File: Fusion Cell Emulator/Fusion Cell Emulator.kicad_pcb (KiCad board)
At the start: 2 copper layers, 116.8 x 190.5 mm, 120 parts, among them J1 BINDING_POST_RED, J2 BINDING_POST_BLACK, J3 JST-XH, J4 0.1" FEMALE HEADER, J6 BINDING_POST_RED, J7 BINDING_POST_BLACK, U1 LM317, U10 LM317, U11 LM317, U12 LM317, U13 LM317, U2 LM317, U3 LM317, U4 LM317, U5 LM317, U6 LM317, U7 LM317, U8 LM317, U9 LM317

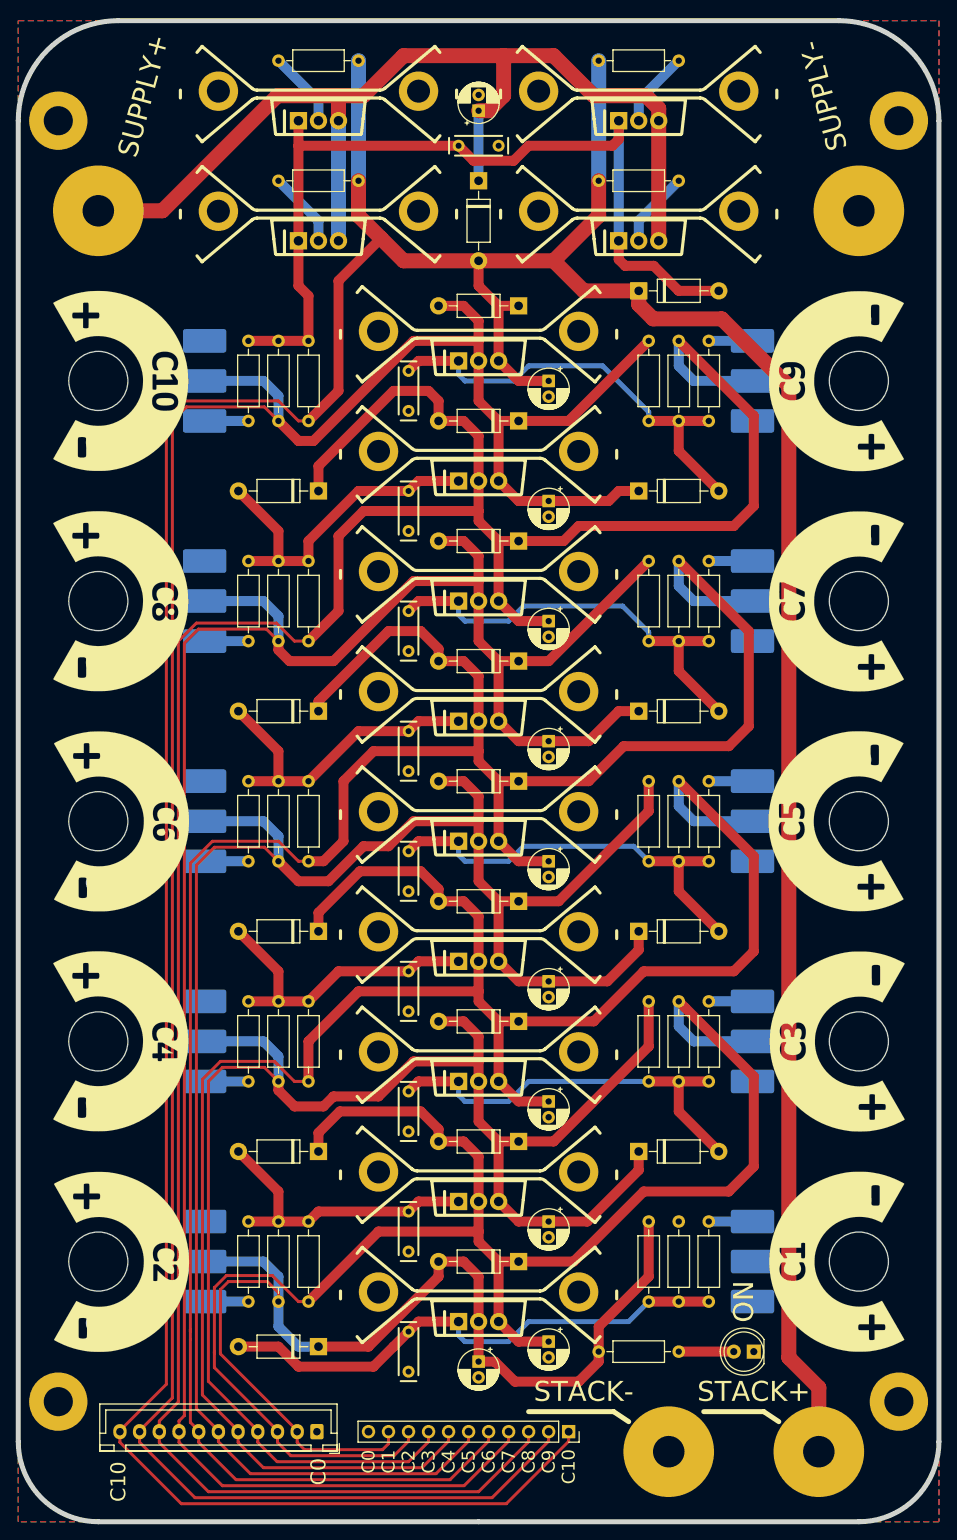
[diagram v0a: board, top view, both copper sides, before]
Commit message: Fixing silk screen and updating gerbers
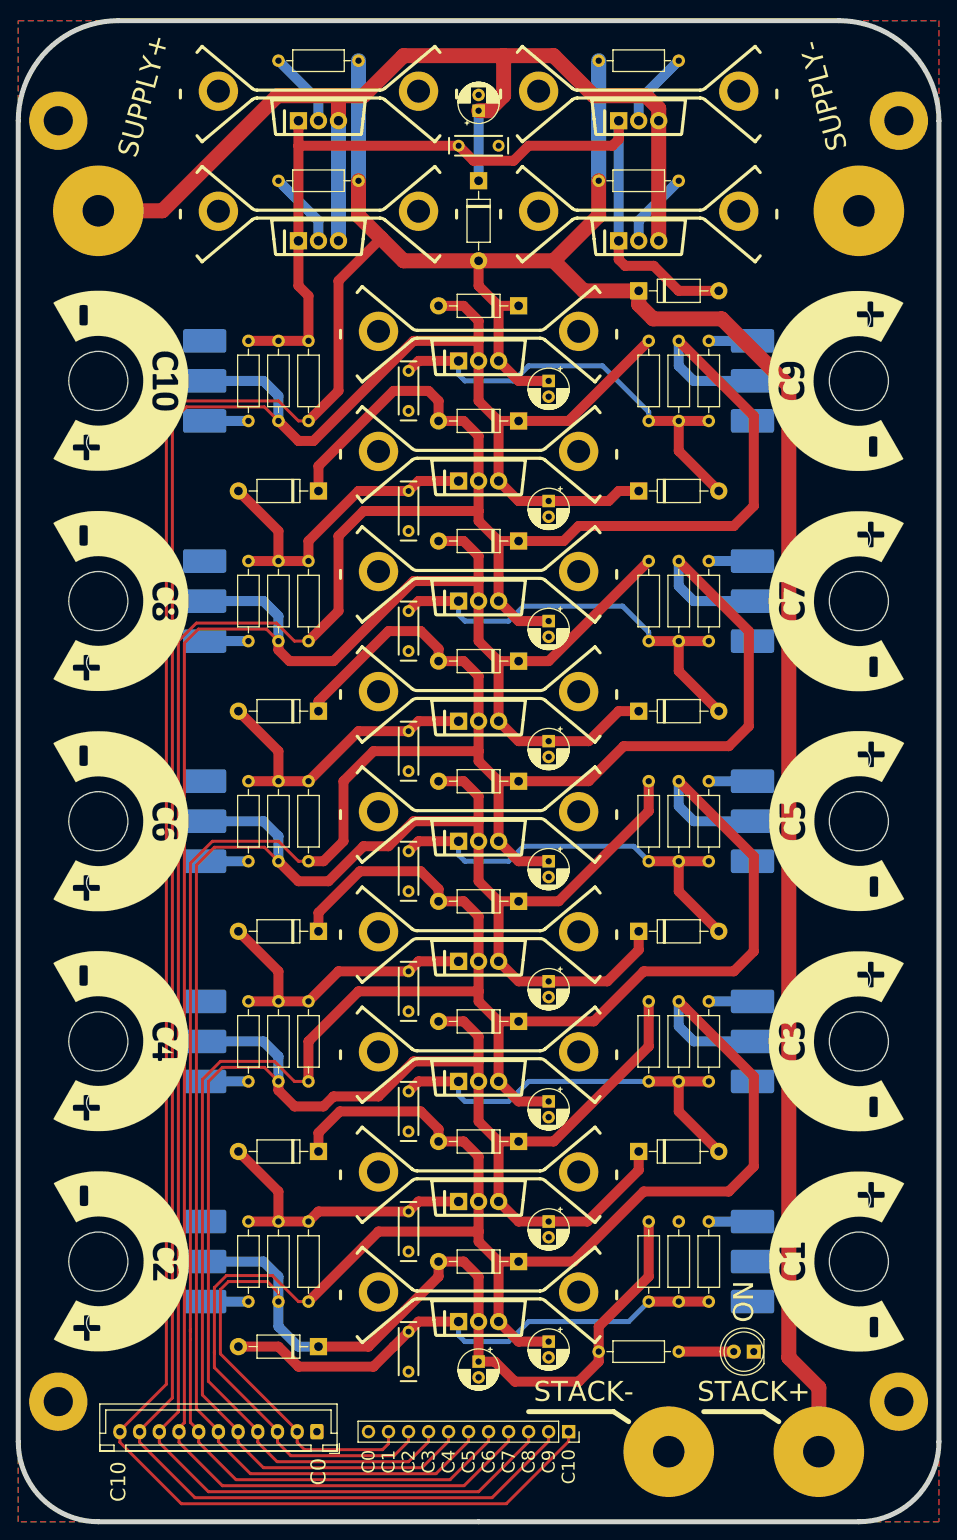
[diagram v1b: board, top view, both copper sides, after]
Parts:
- removed the G*** at (201.0, 103.2)
- removed the G*** at (103.8, -6.70)
- removed the G*** at (201.1, 75.3)
- removed the G*** at (200.9, 47.4)
- removed the G*** at (200.9, 19.4)
- removed the G*** at (200.9, -8.50)
- removed the G*** at (104.0, 105.1)
- removed the G*** at (103.8, 77.1)
- removed the G*** at (104.0, 49.2)
- removed the G*** at (103.8, 21.2)
- added G***: LOGO, Custom-Graphics:Cell_Graphic_Invert_C1, F.Cu at (200.9, 105.0)
- added G***: LOGO, Custom-Graphics:Cell_Graphic_Invert_C10, F.Cu at (104.0, -8.45)
- added G***: LOGO, Custom-Graphics:Cell_Graphic_Invert_C3, F.Cu at (200.8, 77.0)
- added G***: Cell_Graphic_Invert_C5, Custom-Graphics:Cell_Graphic_Invert_C5, F.Cu at (200.9, 49.0)
- added G***: LOGO, Custom-Graphics:Cell_Graphic_Invert_C7, F.Cu at (200.8, 21.1)
- added G***: LOGO, Custom-Graphics:Cell_Graphic_Invert_C9, F.Cu at (200.8, -6.80)
- added G***: LOGO, Custom-Graphics:Cell_Graphic_Invert_C2, F.Cu at (104.0, 103.3)
- added G***: LOGO, Custom-Graphics:Cell_Graphic_Invert_C4, F.Cu at (104.0, 75.3)
- added G***: LOGO, Custom-Graphics:Cell_Graphic_Invert_C6, F.Cu at (104.0, 47.5)
- added G***: LOGO, Custom-Graphics:Cell_Graphic_Invert_C8, F.Cu at (104.0, 19.5)

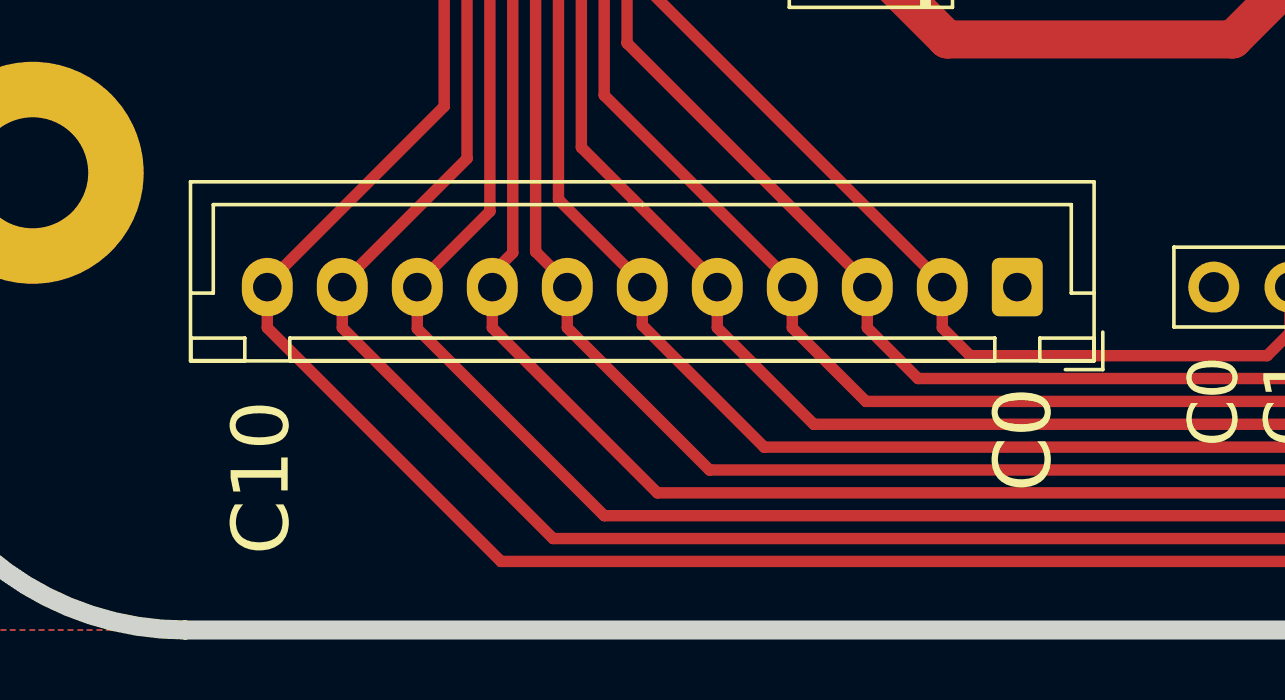
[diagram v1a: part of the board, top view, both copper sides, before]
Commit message: Fixed JST orietation and Final Gerbers
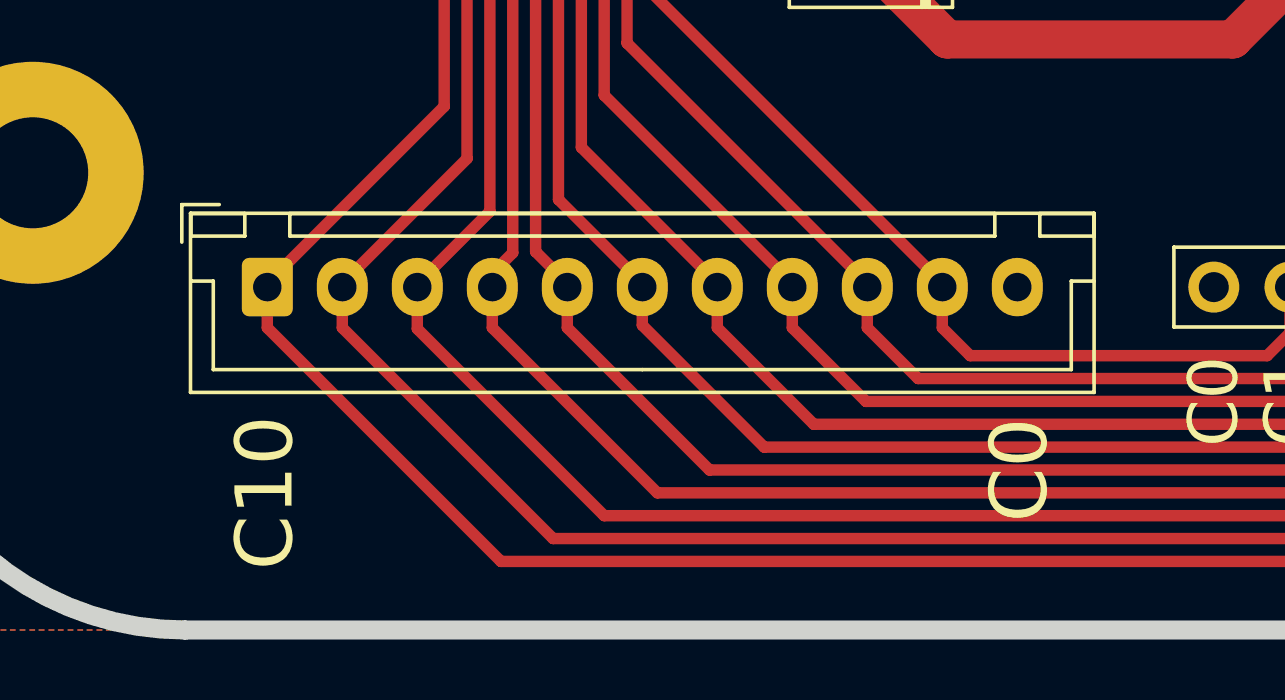
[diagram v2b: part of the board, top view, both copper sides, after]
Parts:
- moved J3 25.0 mm to (106.9, 125.7), turned to 0 degrees
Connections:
- J3 pad 1: GND -> /C10
- J3 pad 10: /C9 -> /C1
- J3 pad 11: /C10 -> GND
- J3 pad 2: /C1 -> /C9
- J3 pad 3: /C2 -> /C8
- J3 pad 4: /C3 -> /C7
- J3 pad 5: /C4 -> /C6
- J3 pad 7: /C6 -> /C4
- J3 pad 8: /C7 -> /C3
- J3 pad 9: /C8 -> /C2
